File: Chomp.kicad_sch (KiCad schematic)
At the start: 49 parts, among them J1 IN2, J10 V2-5, J11 L1-1, J12 V2-8, J13 L1-2, J14 V2-6, J15 T2-G, J16 T2-B, J2 IN1, J3 V1-2, J4 V1-1, J5 V1-3, J6 RV1-1, J7 RV1-3, J8 V1-6, J9 V1-8

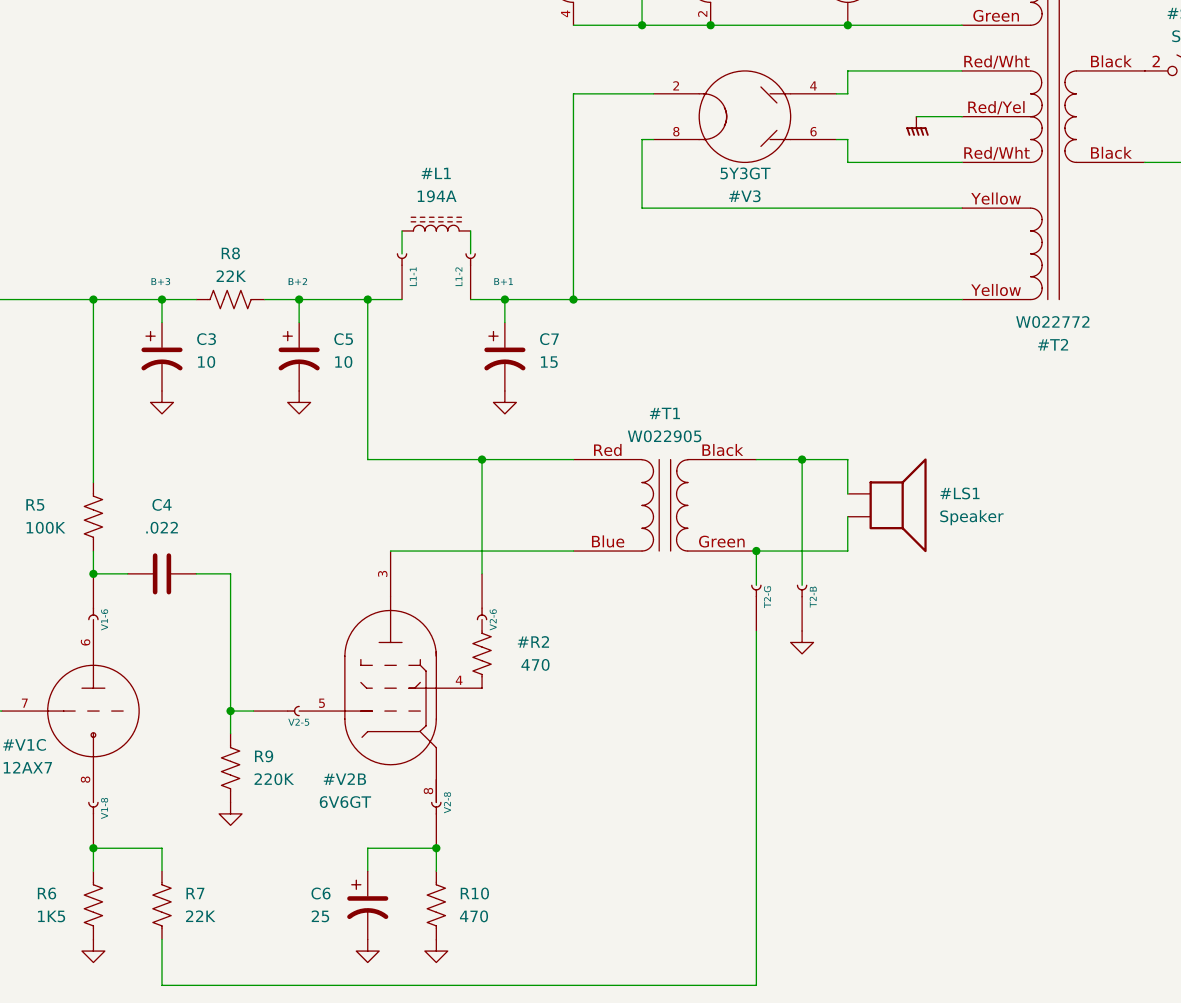
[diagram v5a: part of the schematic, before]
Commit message: Simplify choke wiring.
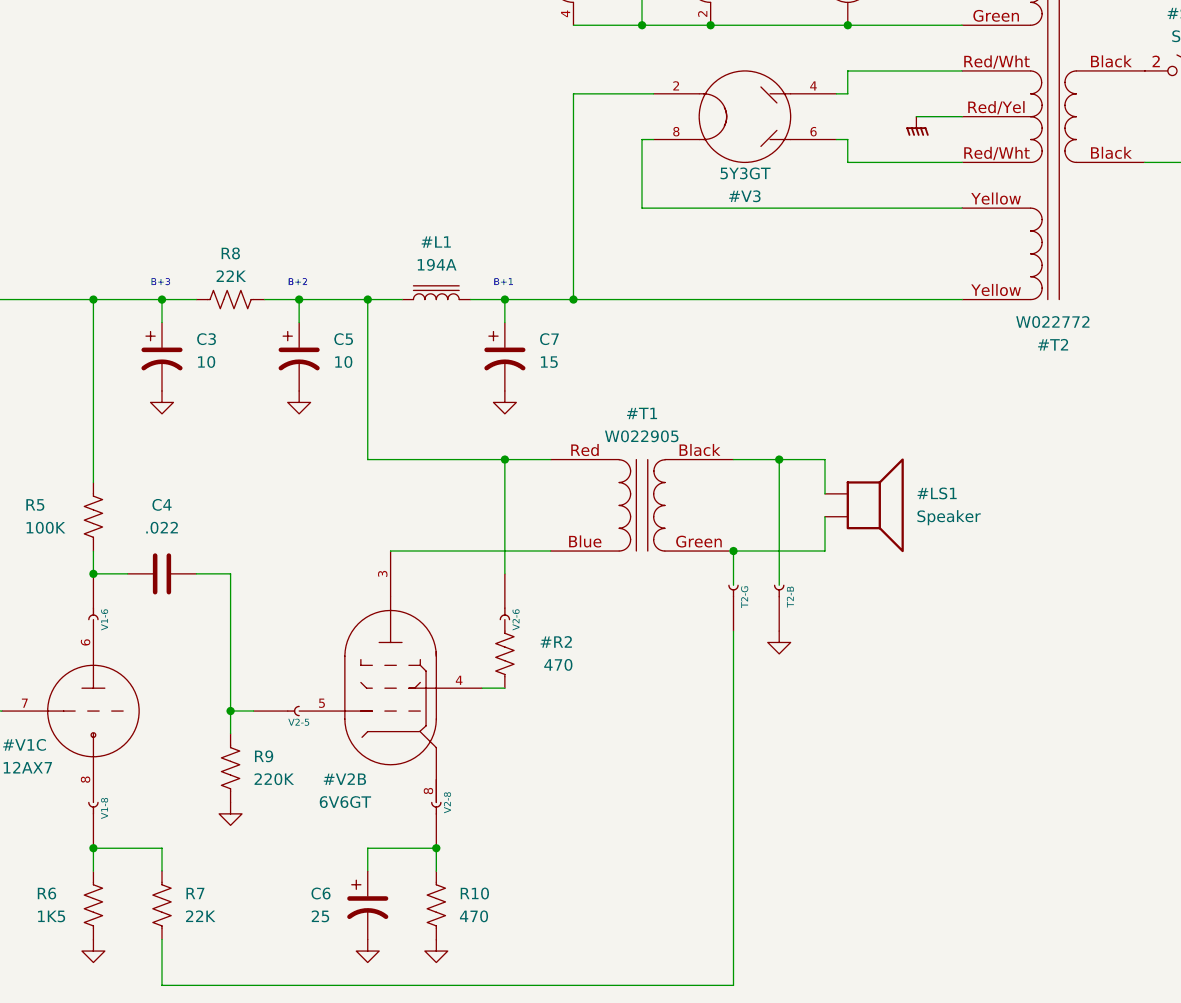
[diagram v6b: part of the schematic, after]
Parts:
- removed J11: L1-1, Connector_Wire:SolderWire-0.25sqmm_1x01_D0.65mm_OD1.7mm, symbol Connector:Conn_01x01_Female
- removed J13: L1-2, Connector_Wire:SolderWire-0.25sqmm_1x01_D0.65mm_OD1.7mm, symbol Connector:Conn_01x01_Female
- #L1: symbol Device:L_Ferrite -> Device:L_Iron
- renumbered J12 to J11, J14 to J12, J15 to J13, J16 to J14
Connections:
- net at #T2.Yellow (OUT2B), #V3.2 (H1), C7.1: now also #L1.2
- net at #T1.Red (AB), C5.1, J12.1 (Pin_1)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: now also #L1.1
